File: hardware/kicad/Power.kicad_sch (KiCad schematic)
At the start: 53 parts, among them J19 USB_C_Receptacle_USB2.0_16P, Q1 FDN304PZ, SW1 SW_SPDT_321, U2 TLV74333PDBVR, U3 TLV74333PDBVR, U6 MCP73871-2CC

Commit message: nothing
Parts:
- removed R3, R4: 10KΩ, symbol Device:R
- added R34, R35: 33KΩ, symbol Device:R
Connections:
- net +BATT: now also R34.1
- net +BATT_PROC: now also D1.1 (K), Q1.2 (S); no longer SW1.3 (A)
- net +VCOM: now also SW1.3 (A); no longer C43.1, U6.1 (OUT), U6.20 (OUT)
- net BATTERY_PERCENTAGE: now also R34.2, R35.1
- net GND: now also R35.2
- removed net +BATT_POLA: D1.1 (K), Q1.2 (S), SW1.2 (B)
- new net +MCP_OUT: C43.1, SW1.2 (B), U6.1 (OUT), U6.20 (OUT)
- no-connect marks 27 -> 21
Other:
- note added: "POLARITY PROTECTION"
- note added: "SWITCHING"
- note removed: "POLARITY PROTECTION AND SWITCHING"
- moved on the sheet: R24, R25, R26, SW1

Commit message: minor changes
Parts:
- removed J19: USB_C_Receptacle_USB2.0_16P, Connector_USB:USB_C_Receptacle_GCT_USB4105-xx-A_16P_TopMnt_Horizontal, symbol Connector:USB_C_Receptacle_USB2.0_16P
- added J1: USB_C_Receptacle_USB2.0_16P, Package_TO_SOT_SMD:SOT-563, symbol Connector:USB_C_Receptacle_USB2.0_16P
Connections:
- net +VUSB: now also J1.A4 (VBUS), J1.A9 (VBUS), J1.B4 (VBUS), J1.B9 (VBUS)
- net CC1: now also J1.A5 (CC1)
- net CC2: now also J1.B5 (CC2)
- net GND: now also J1.A1 (GND), J1.A12 (GND), J1.B1 (GND), J1.B12 (GND), J1.SH (SHIELD)
- no-connect marks 21 -> 19

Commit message: finished schematics
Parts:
- removed U2, U3: TLV74333PDBVR, Package_TO_SOT_SMD:SOT-23-5_HandSoldering, symbol TLV74333PDBVR:TLV74333PDBVR
- added U10, U4: TLV74333PDBVR, Package_TO_SOT_SMD:SOT-23-5_HandSoldering, symbol TLV74333PDBVR:TLV74333PDBVR
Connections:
- net +5V: now also U10.1 (VIN), U10.3 (EN), U4.1 (VIN), U4.3 (EN)
- net +CRYPT_3V3: now also U10.5 (OUT)
- net +STM_3V3: now also U4.5 (OUT)
- net GND: now also U10.2 (GND), U4.2 (GND)
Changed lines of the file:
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@@
 	)
 	(symbol
-		(lib_id "TLV74333PDBVR:TLV74333PDBVR")
-		(at 245.11 33.02 0)
-		(unit 1)
-		(body_style 1)
-		(exclude_from_sim no)
-		(in_bom yes)
-		(on_board yes)
-		(in_pos_files yes)
-		(dnp no)
-		(fields_autoplaced yes)
-		(property "Reference" "U2"
-			(at 245.11 22.86 0)
-			(show_name no)
-			(do_not_autoplace no)
-			(effects
-				(font
-					(size 1.27 1.27)
-				)
-			)
-		)
-		(property "Value" "TLV74333PDBVR"
-			(at 245.11 25.4 0)
-			(show_name no)
-			(do_not_autoplace no)
-			(effects
-				(font
-					(size 1.27 1.27)
-				)
-			)
-		)
-		(property "Footprint" "Package_TO_SOT_SMD:SOT-23-5_HandSoldering"
-			(at 246.38 52.07 0)
-			(hide yes)
-			(show_name no)
-			(do_not_autoplace no)
-			(effects
-				(font
-					(size 1.27 1.27)
-				)
-			)
-		)
-		(property "Datasheet" ""
-			(at 245.11 33.02 0)
-			(hide yes)
-			(show_name no)
-			(do_not_autoplace no)
-			(effects
-				(font
-					(size 1.27 1.27)
-				)
-			)
-		)
-		(property "Description" ""
-			(at 245.11 33.02 0)
-			(hide yes)
-			(show_name no)
-			(do_not_autoplace no)
-			(effects
-				(font
-					(size 1.27 1.27)
-				)
-			)
-		)
-		(pin "5"
-		)
-		(pin "4"
-		)
-		(pin "1"
-		)
-		(pin "2"
-		)
-		(pin "3"
-		)
-		(instances
-			(project "crypto_node"
-				(path "/6c72b0cb-17b9-42a6-811c-297d0c354af3/0878dbd6-f23a-45b7-803f-70f55a38d748"
-					(reference "U2")
-					(unit 1)
-				)
-			)
-		)
-	)
-	(symbol
 		(lib_id "power:+BATT")
 		(at 148.59 69.85 0)
@@
 	)
 	(symbol
-		(lib_id "TLV74333PDBVR:TLV74333PDBVR")
-		(at 245.11 74.93 0)
-		(unit 1)
-		(body_style 1)
-		(exclude_from_sim no)
-		(in_bom yes)
-		(on_board yes)
-		(in_pos_files yes)
-		(dnp no)
-		(fields_autoplaced yes)
-		(property "Reference" "U3"
-			(at 245.11 64.77 0)
-			(show_name no)
-			(do_not_autoplace no)
-			(effects
-				(font
-					(size 1.27 1.27)
-				)
-			)
-		)
-		(property "Value" "TLV74333PDBVR"
-			(at 245.11 67.31 0)
-			(show_name no)
-			(do_not_autoplace no)
-			(effects
-				(font
-					(size 1.27 1.27)
-				)
-			)
-		)
-		(property "Footprint" "Package_TO_SOT_SMD:SOT-23-5_HandSoldering"
-			(at 246.38 93.98 0)
-			(hide yes)
-			(show_name no)
-			(do_not_autoplace no)
-			(effects
-				(font
-					(size 1.27 1.27)
-				)
-			)
-		)
-		(property "Datasheet" ""
-			(at 245.11 74.93 0)
-			(hide yes)
-			(show_name no)
-			(do_not_autoplace no)
-			(effects
-				(font
-					(size 1.27 1.27)
-				)
-			)
-		)
-		(property "Description" ""
-			(at 245.11 74.93 0)
-			(hide yes)
-			(show_name no)
-			(do_not_autoplace no)
-			(effects
-				(font
-					(size 1.27 1.27)
-				)
-			)
-		)
-		(pin "5"
-		)
-		(pin "4"
-		)
-		(pin "1"
-		)
-		(pin "2"
-		)
-		(pin "3"
-		)
-		(instances
-			(project "crypto_node"
-				(path "/6c72b0cb-17b9-42a6-811c-297d0c354af3/0878dbd6-f23a-45b7-803f-70f55a38d748"
-					(reference "U3")
-					(unit 1)
-				)
-			)
-		)
-	)
-	(symbol
 		(lib_id "Device:R")
 		(at 83.82 156.21 0)
@@
 	)
 	(symbol
+		(lib_id "TLV74333PDBVR:TLV74333PDBVR")
+		(at 245.11 74.93 0)
+		(unit 1)
+		(body_style 1)
+		(exclude_from_sim no)
+		(in_bom yes)
+		(on_board yes)
+		(in_pos_files yes)
+		(dnp no)
+		(fields_autoplaced yes)
+		(property "Reference" "U10"
+			(at 245.11 64.77 0)
+			(show_name no)
+			(do_not_autoplace no)
+			(effects
+				(font
+					(size 1.27 1.27)
+				)
+			)
+		)
+		(property "Value" "TLV74333PDBVR"
+			(at 245.11 67.31 0)
+			(show_name no)
+			(do_not_autoplace no)
+			(effects
+				(font
+					(size 1.27 1.27)
+				)
+			)
+		)
+		(property "Footprint" "Package_TO_SOT_SMD:SOT-23-5_HandSoldering"
+			(at 246.38 93.98 0)
+			(hide yes)
+			(show_name no)
+			(do_not_autoplace no)
+			(effects
+				(font
+					(size 1.27 1.27)
+				)
+			)
+		)
+		(property "Datasheet" ""
+			(at 245.11 74.93 0)
+			(hide yes)
+			(show_name no)
+			(do_not_autoplace no)
+			(effects
+				(font
+					(size 1.27 1.27)
+				)
+			)
+		)
+		(property "Description" ""
+			(at 245.11 74.93 0)
+			(hide yes)
+			(show_name no)
+			(do_not_autoplace no)
+			(effects
+				(font
+					(size 1.27 1.27)
+				)
+			)
+		)
+		(pin "2"
+		)
+		(pin "5"
+		)
+		(pin "4"
+		)
+		(pin "1"
+		)
+		(pin "3"
+		)
+		(instances
+			(project "crypto_node"
+				(path "/6c72b0cb-17b9-42a6-811c-297d0c354af3/0878dbd6-f23a-45b7-803f-70f55a38d748"
+					(reference "U10")
+					(unit 1)
+				)
+			)
+		)
+	)
+	(symbol
 		(lib_id "Device:R")
 		(at 86.36 76.2 0)
@@
 					(unit 1)
 				)
+			)
+		)
+	)
+	(symbol
+		(lib_id "TLV74333PDBVR:TLV74333PDBVR")
+		(at 245.11 33.02 0)
+		(unit 1)
+		(body_style 1)
+		(exclude_from_sim no)
+		(in_bom yes)
+		(on_board yes)
+		(in_pos_files yes)
+		(dnp no)
+		(fields_autoplaced yes)
+		(property "Reference" "U4"
+			(at 245.11 22.86 0)
+			(show_name no)
+			(do_not_autoplace no)
+			(effects
+				(font
+					(size 1.27 1.27)
+				)
+			)
+		)
+		(property "Value" "TLV74333PDBVR"
+			(at 245.11 25.4 0)
+			(show_name no)
+			(do_not_autoplace no)
+			(effects
+				(font
+					(size 1.27 1.27)
+				)
+			)
+		)
+		(property "Footprint" "Package_TO_SOT_SMD:SOT-23-5_HandSoldering"
+			(at 246.38 52.07 0)
+			(hide yes)
+			(show_name no)
+			(do_not_autoplace no)
+			(effects
+				(font
+					(size 1.27 1.27)
+				)
+			)
+		)
+		(property "Datasheet" ""
+			(at 245.11 33.02 0)
+			(hide yes)
+			(show_name no)
+			(do_not_autoplace no)
+			(effects
+				(font
+					(size 1.27 1.27)
+				)
+			)
+		)
+		(property "Description" ""
+			(at 245.11 33.02 0)
+			(hide yes)
+			(show_name no)
+			(do_not_autoplace no)
+			(effects
+				(font
+					(size 1.27 1.27)
+				)
+			)
+		)
+		(pin "2"
+		)
+		(pin "5"
+		)
+		(pin "4"
+		)
+		(pin "1"
+		)
+		(pin "3"
+		)
+		(instances
+			(project "crypto_node"
+				(path "/6c72b0cb-17b9-42a6-811c-297d0c354af3/0878dbd6-f23a-45b7-803f-70f55a38d748"
+					(reference "U4")
+					(unit 1)
+				)

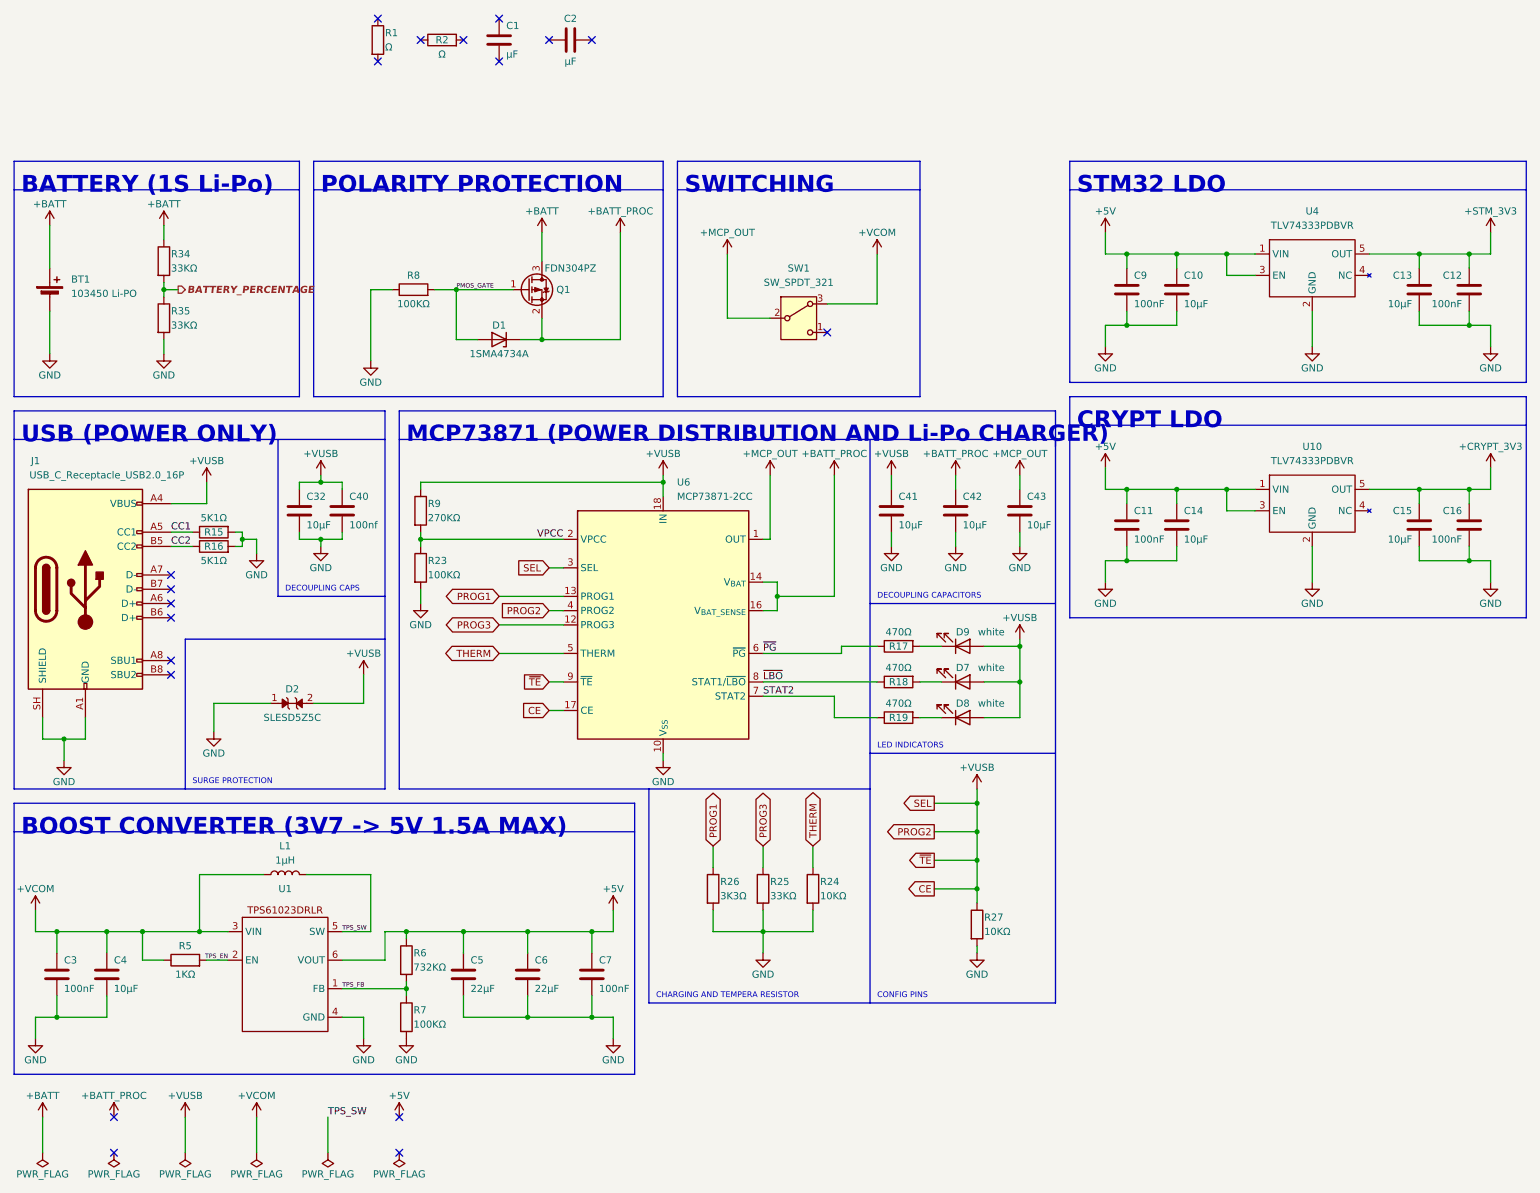
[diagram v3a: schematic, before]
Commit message: schematics refinement
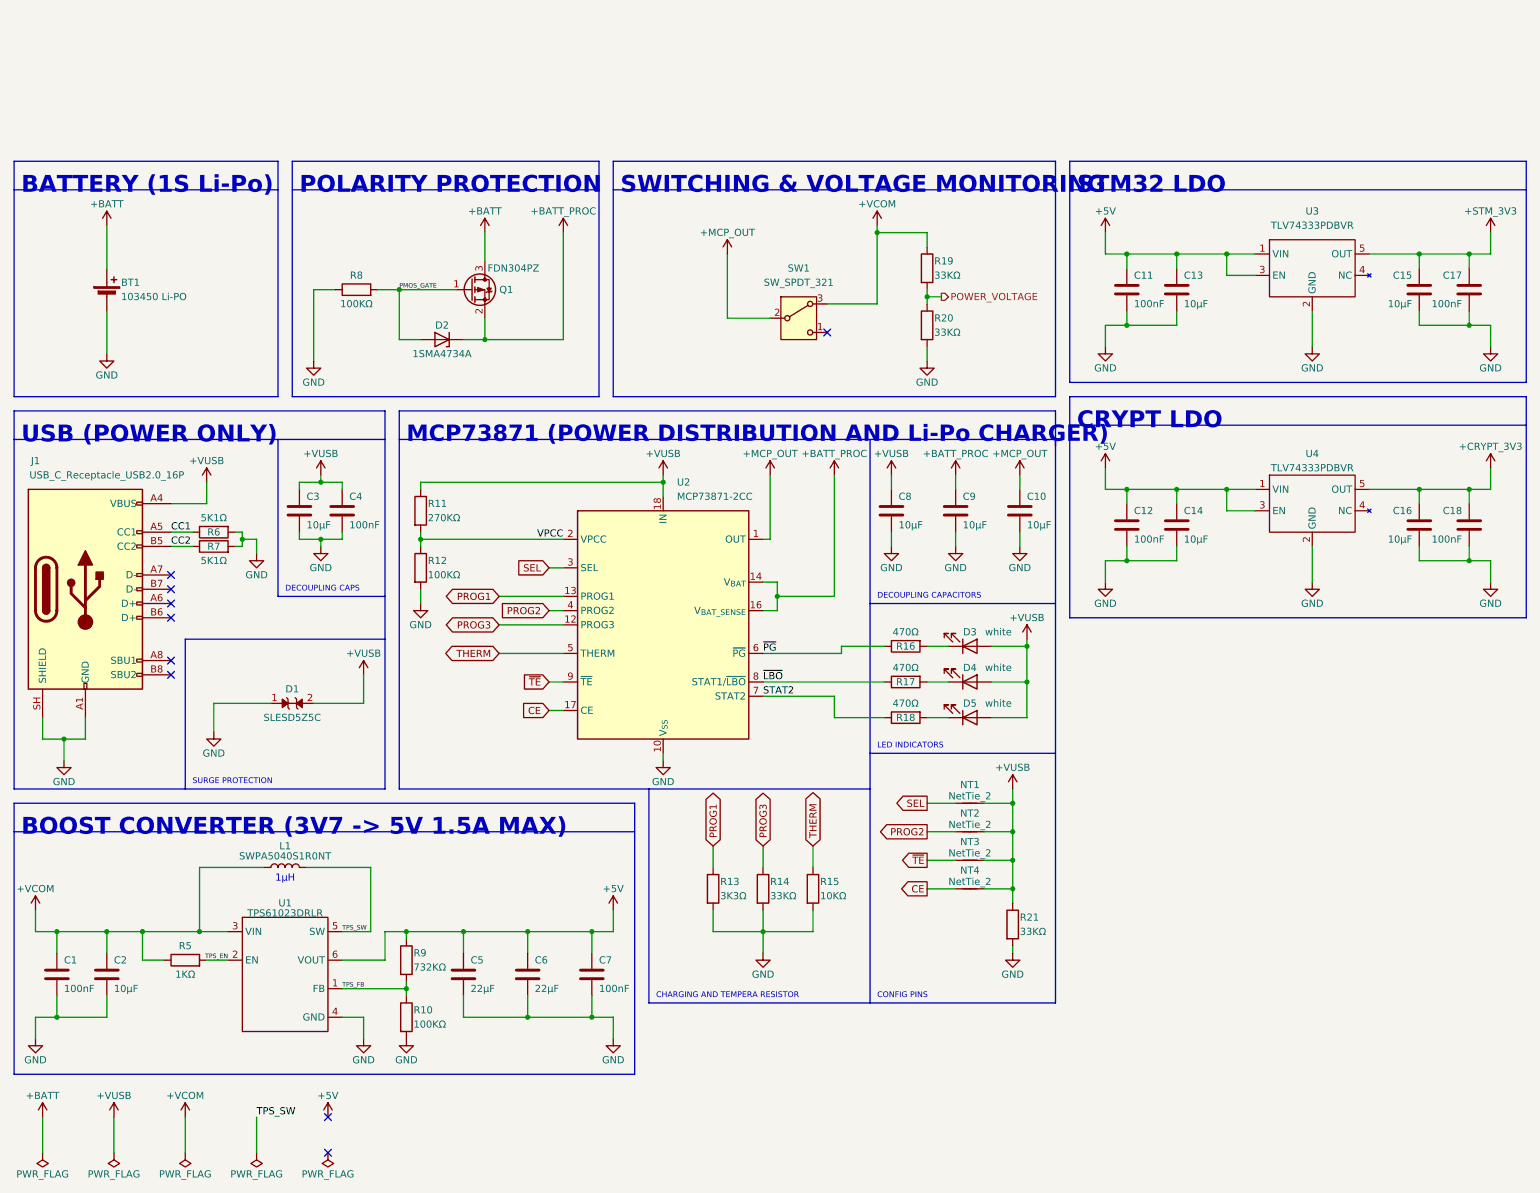
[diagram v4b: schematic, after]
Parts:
- removed C1, C2: μF, symbol Device:C
- removed R1, R2: Ω, symbol Device:R
- removed R27: 10KΩ, symbol Device:R
- removed R34, R35: 33KΩ, symbol Device:R
- added NT1, NT2, NT3, NT4: NetTie_2, NetTie:NetTie-2_SMD_Pad0.5mm, symbol Device:NetTie_2
- added R19, R20, R21: 33KΩ, Resistor_SMD:R_0805_2012Metric_Pad1.20x1.40mm_HandSolder, symbol Device:R
- BT1: footprint (none) -> Connector_JST:JST_PH_B2B-PH-K_1x02_P2.00mm_Vertical
- C1: renamed from C3; footprint (none) -> Capacitor_SMD:C_0603_1608Metric_Pad1.08x0.95mm_HandSolder
- C10: renamed from C43; footprint (none) -> Capacitor_SMD:C_1206_3216Metric_Pad1.33x1.80mm_HandSolder
- C11: renamed from C9; footprint (none) -> Capacitor_SMD:C_0603_1608Metric_Pad1.08x0.95mm_HandSolder
- C12: renamed from C11; footprint (none) -> Capacitor_SMD:C_0603_1608Metric_Pad1.08x0.95mm_HandSolder
- C13: renamed from C10; footprint (none) -> Capacitor_SMD:C_1206_3216Metric_Pad1.33x1.80mm_HandSolder
- C14: footprint (none) -> Capacitor_SMD:C_1206_3216Metric_Pad1.33x1.80mm_HandSolder
- C15: renamed from C13; footprint (none) -> Capacitor_SMD:C_1206_3216Metric_Pad1.33x1.80mm_HandSolder
- C16: renamed from C15; footprint (none) -> Capacitor_SMD:C_1206_3216Metric_Pad1.33x1.80mm_HandSolder
- C17: renamed from C12; footprint (none) -> Capacitor_SMD:C_0603_1608Metric_Pad1.08x0.95mm_HandSolder
- C18: renamed from C16; footprint (none) -> Capacitor_SMD:C_0603_1608Metric_Pad1.08x0.95mm_HandSolder
- C2: renamed from C4; footprint (none) -> Capacitor_SMD:C_1206_3216Metric_Pad1.33x1.80mm_HandSolder
- C3: renamed from C32; footprint (none) -> Capacitor_SMD:C_1206_3216Metric_Pad1.33x1.80mm_HandSolder
- C4: renamed from C40; value 100nf -> 100nF; footprint (none) -> Capacitor_SMD:C_0603_1608Metric_Pad1.08x0.95mm_HandSolder
- C5, C6: footprint (none) -> Capacitor_SMD:C_1210_3225Metric_Pad1.33x2.70mm_HandSolder
- C7: footprint (none) -> Capacitor_SMD:C_0603_1608Metric_Pad1.08x0.95mm_HandSolder
- C8: renamed from C41; footprint (none) -> Capacitor_SMD:C_1206_3216Metric_Pad1.33x1.80mm_HandSolder
- C9: renamed from C42; footprint (none) -> Capacitor_SMD:C_1206_3216Metric_Pad1.33x1.80mm_HandSolder
- D2: renamed from D1; footprint (none) -> Diode_SMD:D_SMA
- D3: renamed from D9; footprint LED_SMD:LED_0603_1608Metric -> LED_SMD:LED_0805_2012Metric_Pad1.15x1.40mm_HandSolder
- D4: renamed from D7; footprint LED_SMD:LED_0603_1608Metric -> LED_SMD:LED_0805_2012Metric_Pad1.15x1.40mm_HandSolder
- D5: renamed from D8; footprint LED_SMD:LED_0603_1608Metric -> LED_SMD:LED_0805_2012Metric_Pad1.15x1.40mm_HandSolder
- J1: footprint Package_TO_SOT_SMD:SOT-563 -> Connector_USB:USB_C_Receptacle_GCT_USB4105-xx-A_16P_TopMnt_Horizontal
- L1: value 1μH -> SWPA5040S1R0NT; footprint (none) -> Inductor_SMD:L_Sunlord_SWPA5040S
- Q1: footprint PCM_SparkFun-Semiconductor-Standard:SOT23-3 -> Package_TO_SOT_SMD:SOT-23
- R10: renamed from R7; footprint (none) -> Resistor_SMD:R_0805_2012Metric_Pad1.20x1.40mm_HandSolder
- R11: renamed from R9; footprint (none) -> Resistor_SMD:R_0805_2012Metric_Pad1.20x1.40mm_HandSolder
- R12: renamed from R23; footprint (none) -> Resistor_SMD:R_0805_2012Metric_Pad1.20x1.40mm_HandSolder
- R13: renamed from R26; footprint (none) -> Resistor_SMD:R_0805_2012Metric_Pad1.20x1.40mm_HandSolder
- R14: renamed from R25; footprint (none) -> Resistor_SMD:R_0805_2012Metric_Pad1.20x1.40mm_HandSolder
- R15: renamed from R24; footprint (none) -> Resistor_SMD:R_0805_2012Metric_Pad1.20x1.40mm_HandSolder
- R16: renamed from R17; footprint (none) -> Resistor_SMD:R_0805_2012Metric_Pad1.20x1.40mm_HandSolder
- R17: renamed from R18; footprint (none) -> Resistor_SMD:R_0805_2012Metric_Pad1.20x1.40mm_HandSolder
- R18: renamed from R19; footprint (none) -> Resistor_SMD:R_0805_2012Metric_Pad1.20x1.40mm_HandSolder
- R5, R8: footprint (none) -> Resistor_SMD:R_0805_2012Metric_Pad1.20x1.40mm_HandSolder
- R6: renamed from R15; footprint (none) -> Resistor_SMD:R_0805_2012Metric_Pad1.20x1.40mm_HandSolder
- R7: renamed from R16; footprint (none) -> Resistor_SMD:R_0805_2012Metric_Pad1.20x1.40mm_HandSolder
- R9: renamed from R6; footprint (none) -> Resistor_SMD:R_0805_2012Metric_Pad1.20x1.40mm_HandSolder
- SW1: footprint (none) -> SS-12D10L7-XKB:SS-12D10L7-XKB
- U1: value (none) -> TPS61023DRLR
- renumbered D2 to D1, U6 to U2, U4 to U3, U10 to U4
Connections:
- net +VCOM: now also R19.1
- net +VUSB: now also NT1.2, NT2.2, NT3.2, NT4.2, R21.1; no longer U2.17 (CE), U2.3 (SEL), U2.4 (PROG2), U2.9 (~{TE})
- net GND: now also R20.2, R21.2
- new net CE: NT4.1, U2.17 (CE)
- new net POWER_VOLTAGE: R19.2, R20.1
- new net PROG2: NT2.1, U2.4 (PROG2)
- new net SEL: NT1.1, U2.3 (SEL)
- new net ~{TE}: NT3.1, U2.9 (~{TE})
- no-connect marks 19 -> 9
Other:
- note added: "1μH"
- note added: "SWITCHING & VOLTAGE MONITORING"
- note removed: "SWITCHING"
- moved on the sheet: BT1, D2, D3, D4, D5, L1, Q1, R16, R17, R18, R8
